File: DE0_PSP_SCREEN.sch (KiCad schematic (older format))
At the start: 11 parts, among them P1 PSP1000LCD, P2 DE0_GPIO_0, P3 DE0_GPIO_1, P4 PSP1000LED

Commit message: More sch
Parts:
- removed C? (x2): 4.7 uF, symbol CP1
- removed C? (x2): 100 n, symbol C
- removed C? (x2): 10 n, symbol C
- removed K?: CONN_3, symbol CONN_3
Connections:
- net labels added: Backlight_dimm, backlight_vcc
- wire segments 89 -> 88
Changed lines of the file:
@@
-EESchema Schematic File Version 2  date Wed 24 Oct 2012 22:22:57 CEST
+EESchema Schematic File Version 2  date Fri 26 Oct 2012 14:46:37 CEST
 LIBS:power
 LIBS:device
@@
 $Descr A4 11693 8268
 encoding utf-8
-Sheet 1 2
+Sheet 1 3
 Title ""
-Date "24 oct 2012"
+Date "26 oct 2012"
 Rev ""
 Comp ""
@@
 	9100 2950 9450 2950
 Wire Wire Line
-	9450 2950 9450 2050
+	9450 2950 9450 2500
+Wire Wire Line
+	9450 2500 9450 2050
 Wire Wire Line
 	9450 2050 9100 2050
@@
 Connection ~ 9450 2500
 Wire Wire Line
-	1700 1350 1700 1450
+	1700 1350 1700 1400
+Wire Wire Line
+	1700 1400 1700 1450
 Wire Wire Line
 	1700 1400 1200 1400
@@
 	2900 1350 3050 1350
 Wire Wire Line
-	3050 1350 3050 1450
+	3050 1350 3050 1400
+Wire Wire Line
+	3050 1400 3050 1450
 Wire Wire Line
 	3050 1400 3200 1400
@@
 	3200 1400 3200 1500
 Wire Wire Line
-	1700 1550 1700 1650
+	1700 1550 1700 1600
+Wire Wire Line
+	1700 1600 1700 1650
 Wire Wire Line
 	1700 1600 1550 1600
@@
 $EndComp
 Wire Wire Line
-	2900 1750 2900 1850
+	2900 1750 2900 1800
+Wire Wire Line
+	2900 1800 2900 1850
 Wire Wire Line
 	2900 1800 3300 1800
@@
 	1    0    0    -1
 $EndComp
-$Comp
-L CONN_3 K?
-U 1 1 5088053C
-P 6650 950
-F 0 "K?" V 6600 950 50  0000 C CNN
-F 1 "CONN_3" V 6700 950 40  0000 C CNN
-	1    6650 950
-	1    0    0    -1
-$EndComp
-Wire Wire Line
-	6300 850  6150 850
-Wire Wire Line
-	6100 950  6300 950
-$Comp
-L +5V #PWR?
-U 1 1 5088064A
-P 6150 850
-F 0 "#PWR?" H 6150 940 20  0001 C CNN
-F 1 "+5V" H 6150 940 30  0000 C CNN
-	1    6150 850
-	1    0    0    -1
-$EndComp
-$Comp
-L +5VA #PWR?
-U 1 1 50880716
-P 6100 950
-F 0 "#PWR?" H 6100 1080 20  0001 C CNN
-F 1 "+5VA" H 6100 1050 30  0000 C CNN
-	1    6100 950
-	1    0    0    -1
-$EndComp
-Wire Wire Line
-	6300 1050 6150 1050
-Wire Wire Line
-	6150 1050 6150 1100
-$Comp
-L GND #PWR?
-U 1 1 508807F0
-P 6150 1100
-F 0 "#PWR?" H 6150 1100 30  0001 C CNN
-F 1 "GND" H 6150 1030 30  0001 C CNN
-	1    6150 1100
-	1    0    0    -1
-$EndComp
-$Comp
-L CP1 C?
-U 1 1 508807FF
-P 2200 6750
-F 0 "C?" H 2250 6850 50  0000 L CNN
-F 1 "4.7 uF" H 2250 6650 50  0000 L CNN
-	1    2200 6750
-	1    0    0    -1
-$EndComp
-$Comp
-L C C?
-U 1 1 5088080E
-P 1900 6750
-F 0 "C?" H 1950 6850 50  0000 L CNN
-F 1 "100 n" H 1950 6650 50  0000 L CNN
-	1    1900 6750
-	1    0    0    -1
-$EndComp
-$Comp
-L C C?
-U 1 1 5088081D
-P 1600 6750
-F 0 "C?" H 1650 6850 50  0000 L CNN
-F 1 "10 n" H 1650 6650 50  0000 L CNN
-	1    1600 6750
-	1    0    0    -1
-$EndComp
-Wire Wire Line
-	1600 6550 2200 6550
-Connection ~ 1900 6550
-Wire Wire Line
-	1600 6950 2200 6950
-Connection ~ 1900 6950
-Wire Wire Line
-	1900 6950 1900 7150
-Wire Wire Line
-	1900 6550 1900 6350
-$Comp
-L +5VA #PWR?
-U 1 1 50880B57
-P 1900 6350
-F 0 "#PWR?" H 1900 6480 20  0001 C CNN
-F 1 "+5VA" H 1900 6450 30  0000 C CNN
-	1    1900 6350
-	1    0    0    -1
-$EndComp
-$Comp
-L GND #PWR?
-U 1 1 50880D2D
-P 1900 7150
-F 0 "#PWR?" H 1900 7150 30  0001 C CNN
-F 1 "GND" H 1900 7080 30  0001 C CNN
-	1    1900 7150
-	1    0    0    -1
-$EndComp
-$Comp
-L CP1 C?
-U 1 1 50880D3A
-P 3350 6750
-F 0 "C?" H 3400 6850 50  0000 L CNN
-F 1 "4.7 uF" H 3400 6650 50  0000 L CNN
-	1    3350 6750
-	1    0    0    -1
-$EndComp
-$Comp
-L C C?
-U 1 1 50880D40
-P 3050 6750
-F 0 "C?" H 3100 6850 50  0000 L CNN
-F 1 "100 n" H 3100 6650 50  0000 L CNN
-	1    3050 6750
-	1    0    0    -1
-$EndComp
-$Comp
-L C C?
-U 1 1 50880D46
-P 2750 6750
-F 0 "C?" H 2800 6850 50  0000 L CNN
-F 1 "10 n" H 2800 6650 50  0000 L CNN
-	1    2750 6750
-	1    0    0    -1
-$EndComp
-Wire Wire Line
-	2750 6550 3350 6550
-Connection ~ 3050 6550
-Wire Wire Line
-	2750 6950 3350 6950
-Connection ~ 3050 6950
-Wire Wire Line
-	3050 6950 3050 7150
-Wire Wire Line
-	3050 6550 3050 6350
-$Comp
-L GND #PWR?
-U 1 1 50880D58
-P 3050 7150
-F 0 "#PWR?" H 3050 7150 30  0001 C CNN
-F 1 "GND" H 3050 7080 30  0001 C CNN
-	1    3050 7150
-	1    0    0    -1
-$EndComp
-$Comp
-L 3V3 #PWR?
-U 1 1 50880D60
-P 3050 6350
-F 0 "#PWR?" H 3050 6450 40  0001 C CNN
-F 1 "3V3" H 3050 6475 40  0000 C CNN
-	1    3050 6350
-	1    0    0    -1
-$EndComp
 $Sheet
 S 5150 6000 1350 950
@@
 F0 "Sheet50883C15" 60
 F1 "file50883C15.sch" 60
+F2 "Vin" I L 5150 6150 60
+F3 "Vout_backlight" I R 6500 6150 60
+F4 "backlight_dimm" I L 5150 6300 60
+$EndSheet
+Wire Wire Line
+	1750 4000 1500 4000
+Wire Wire Line
+	1500 4000 1500 4050
+$Comp
+L GND #PWR?
+U 1 1 508A54D8
+P 1500 4050
+F 0 "#PWR?" H 1500 4050 30  0001 C CNN
+F 1 "GND" H 1500 3980 30  0001 C CNN
+	1    1500 4050
+	1    0    0    -1
+$EndComp
+Wire Wire Line
+	1750 4300 1600 4300
+Text Label 6500 6150 0    60   ~ 0
+backlight_vcc
+Text Label 1600 4300 2    60   ~ 0
+backlight_vcc
+Text Label 5150 6300 2    60   ~ 0
+Backlight_dimm
+Text Label 9250 4250 0    60   ~ 0
+Backlight_dimm
+Wire Wire Line
+	9100 4250 9250 4250
+Wire Wire Line
+	5150 6150 4950 6150
+Wire Wire Line
+	4950 6150 4950 6100
+$Comp
+L +5VA #PWR?
+U 1 1 508A5F9C
+P 4950 6100
+F 0 "#PWR?" H 4950 6230 20  0001 C CNN
+F 1 "+5VA" H 4950 6200 30  0000 C CNN
+	1    4950 6100
+	1    0    0    -1
+$EndComp
+$Sheet
+S 5250 3550 1300 1100
+U 508A654A
+F0 "Sheet508A6549" 60
+F1 "file508A6549.sch" 60
 $EndSheet
 $EndSCHEMATC

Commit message: Added power supply
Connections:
- net labels added: 3v3ENA, 3v3Vreg, 5Vreg, 5vENA, DE0_3v3, DE0_5v
- net labels removed: +5V, +5VA, 3V3
- wire segments 88 -> 90
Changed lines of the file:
@@
-EESchema Schematic File Version 2  date Fri 26 Oct 2012 14:46:37 CEST
+EESchema Schematic File Version 2  date Sun 28 Oct 2012 15:35:36 CET
 LIBS:power
 LIBS:device
@@
 Sheet 1 3
 Title ""
-Date "26 oct 2012"
+Date "28 oct 2012"
 Rev ""
 Comp ""
@@
 Comment4 ""
 $EndDescr
-$Comp
-L PSP1000LCD P1
-U 1 1 5086F785
-P 2300 2300
-F 0 "P1" H 2300 3400 70  0000 C CNN
-F 1 "PSP1000LCD" H 2300 1200 70  0000 C CNN
-	1    2300 2300
-	1    0    0    -1
-$EndComp
 Text Label 1550 1750 0    60   ~ 0
 R0
@@
 Text Label 3050 2050 2    60   ~ 0
 Vsync
-Text Label 9250 4050 2    60   ~ 0
+Text Label 9250 4050 0    60   ~ 0
 CK
-Text Label 8150 4150 0    60   ~ 0
+Text Label 8150 4150 2    60   ~ 0
 DISP
-Text Label 9250 4150 2    60   ~ 0
+Text Label 9250 4150 0    60   ~ 0
 Hsync
-Text Label 8150 4250 0    60   ~ 0
+Text Label 8150 4250 2    60   ~ 0
 Vsync
 $Comp
@@
 	1    0    0    -1
 $EndComp
-$Comp
-L 3V3 #PWR05
-U 1 1 5087FF71
-P 1550 1600
-F 0 "#PWR05" H 1550 1700 40  0001 C CNN
-F 1 "3V3" H 1550 1725 40  0000 C CNN
-	1    1550 1600
-	1    0    0    -1
-$EndComp
 Wire Wire Line
 	1700 1750 1550 1750
@@
 	9100 2850 9250 2850
 Wire Wire Line
-	9100 2950 9450 2950
-Wire Wire Line
-	9450 2950 9450 2500
-Wire Wire Line
-	9450 2500 9450 2050
+	9450 2950 9100 2950
+Wire Wire Line
+	9450 2050 9450 2950
 Wire Wire Line
 	9450 2050 9100 2050
@@
 Connection ~ 9450 2500
 Wire Wire Line
-	1700 1350 1700 1400
-Wire Wire Line
-	1700 1400 1700 1450
+	1700 1350 1700 1450
 Wire Wire Line
 	1700 1400 1200 1400
@@
 	8300 4250 8150 4250
 Wire Wire Line
-	2900 1450 3050 1450
+	3050 1450 2900 1450
 Wire Wire Line
 	2900 1350 3050 1350
 Wire Wire Line
-	3050 1350 3050 1400
-Wire Wire Line
-	3050 1400 3050 1450
+	3050 1350 3050 1450
 Wire Wire Line
 	3050 1400 3200 1400
@@
 	3200 1400 3200 1500
 Wire Wire Line
-	1700 1550 1700 1600
-Wire Wire Line
-	1700 1600 1700 1650
+	1700 1550 1700 1650
 Wire Wire Line
 	1700 1600 1550 1600
@@
 Wire Wire Line
 	8300 2950 8000 2950
-$Comp
-L 3V3 #PWR06
-U 1 1 5088002D
-P 8000 2950
-F 0 "#PWR06" H 8000 3050 40  0001 C CNN
-F 1 "3V3" H 8000 3075 40  0000 C CNN
-	1    8000 2950
-	1    0    0    -1
-$EndComp
 $Comp
 L PSP1000LED P4
@@
 $EndComp
 Wire Wire Line
-	2900 1750 2900 1800
-Wire Wire Line
-	2900 1800 2900 1850
+	2900 1750 2900 1850
 Wire Wire Line
 	2900 1800 3300 1800
 Connection ~ 2900 1800
-$Comp
-L +5VA #PWR?
-U 1 1 508804CB
-P 3300 1800
-F 0 "#PWR?" H 3300 1930 20  0001 C CNN
-F 1 "+5VA" H 3300 1900 30  0000 C CNN
-	1    3300 1800
-	1    0    0    -1
-$EndComp
 Wire Wire Line
 	8300 2050 8000 2050
-$Comp
-L +5V #PWR?
-U 1 1 5088052D
-P 8000 2050
-F 0 "#PWR?" H 8000 2140 20  0001 C CNN
-F 1 "+5V" H 8000 2140 30  0000 C CNN
-	1    8000 2050
-	1    0    0    -1
-$EndComp
 $Sheet
 S 5150 6000 1350 950
@@
 	1500 4000 1500 4050
 $Comp
-L GND #PWR?
+L GND #PWR05
 U 1 1 508A54D8
 P 1500 4050
-F 0 "#PWR?" H 1500 4050 30  0001 C CNN
+F 0 "#PWR05" H 1500 4050 30  0001 C CNN
 F 1 "GND" H 1500 3980 30  0001 C CNN
 	1    1500 4050
@@
 Wire Wire Line
 	4950 6150 4950 6100
-$Comp
-L +5VA #PWR?
-U 1 1 508A5F9C
-P 4950 6100
-F 0 "#PWR?" H 4950 6230 20  0001 C CNN
-F 1 "+5VA" H 4950 6200 30  0000 C CNN
-	1    4950 6100
-	1    0    0    -1
-$EndComp
 $Sheet
 S 5250 3550 1300 1100
@@
 F0 "Sheet508A6549" 60
 F1 "file508A6549.sch" 60
+F2 "V6-24" I L 5250 3700 60
+F3 "DE0_5v" I L 5250 3850 60
+F4 "DE0_3v3" I L 5250 4000 60
+F5 "5Vreg" I R 6550 3700 60
+F6 "3v3Vreg" I R 6550 3850 60
+F7 "5vENA" I L 5250 4250 60
+F8 "3v3ENA" I L 5250 4400 60
 $EndSheet
+Text Label 6550 3700 0    60   ~ 0
+5Vreg
+Text Label 3300 1800 0    60   ~ 0
+5Vreg
+Text Label 6550 3850 0    60   ~ 0
+3v3Vreg
+$Comp
+L PSP1000LCD P1
+U 1 1 5086F785
+P 2300 2300
+F 0 "P1" H 2300 3400 70  0000 C CNN
+F 1 "PSP1000LCD" H 2300 1200 70  0000 C CNN
+	1    2300 2300
+	1    0    0    -1
+$EndComp
+Text Label 1550 1600 2    60   ~ 0
+3v3Vreg
+Text Label 4950 6100 2    60   ~ 0
+5Vreg
+Text Label 8000 2950 2    60   ~ 0
+DE0_3v3
+Text Label 5250 4000 2    60   ~ 0
+DE0_3v3
+Text Label 8000 2050 2    60   ~ 0
+DE0_5v
+Text Label 5250 3850 2    60   ~ 0
+DE0_5v
+Text Label 5250 4250 2    60   ~ 0
+5vENA
+Text Label 5250 4400 2    60   ~ 0
+3v3ENA
+Wire Wire Line
+	8300 4350 8150 4350
+Wire Wire Line
+	9100 4350 9250 4350
+Text Label 9250 4350 0    60   ~ 0
+5vENA
+Text Label 8150 4350 2    60   ~ 0
+3v3ENA
+Wire Wire Line
+	9100 4550 9550 4550
+Wire Wire Line
+	9550 4550 9550 5450
+Wire Wire Line
+	9550 5450 9100 5450
+Wire Wire Line
+	9550 5000 9900 5000
+Wire Wire Line
+	9900 5000 9900 5250
+Connection ~ 9550 5000
+$Comp
+L GND #PWR06
+U 1 1 508D5FD4
+P 9900 5250
+F 0 "#PWR06" H 9900 5250 30  0001 C CNN
+F 1 "GND" H 9900 5180 30  0001 C CNN
+	1    9900 5250
+	1    0    0    -1
+$EndComp
 $EndSCHEMATC

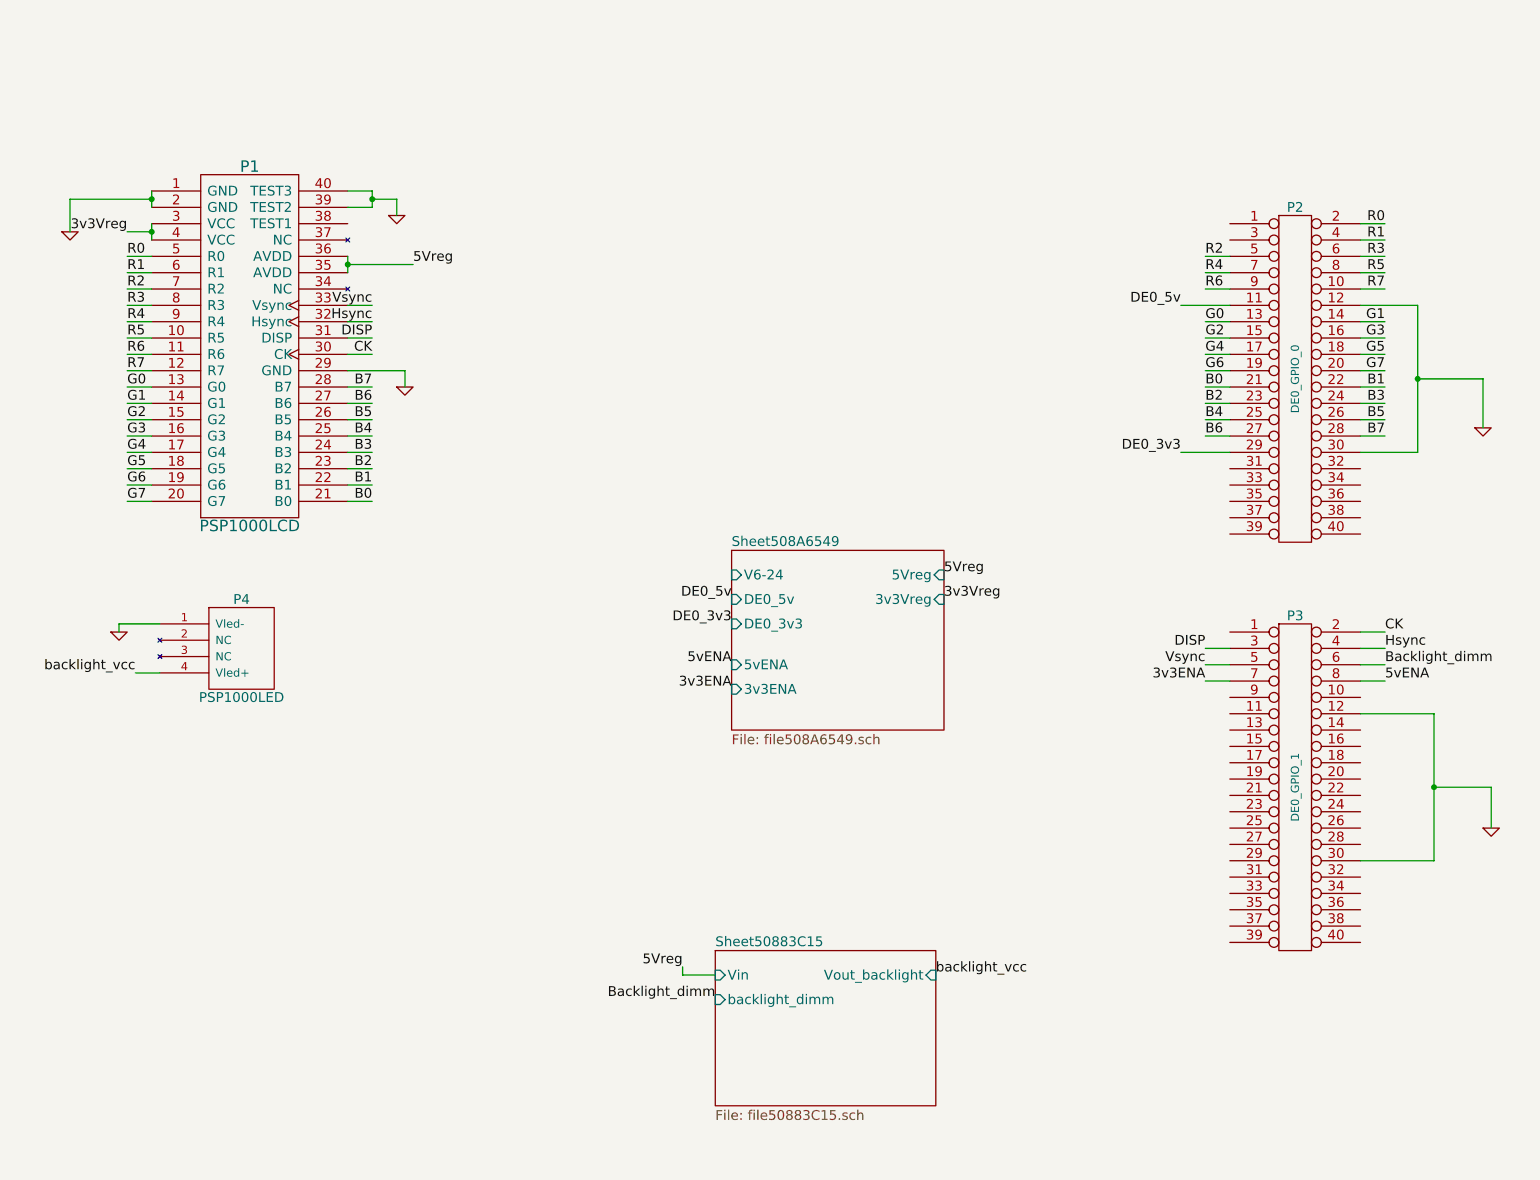
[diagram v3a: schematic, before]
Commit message: Added micro sd to main sch and more routing
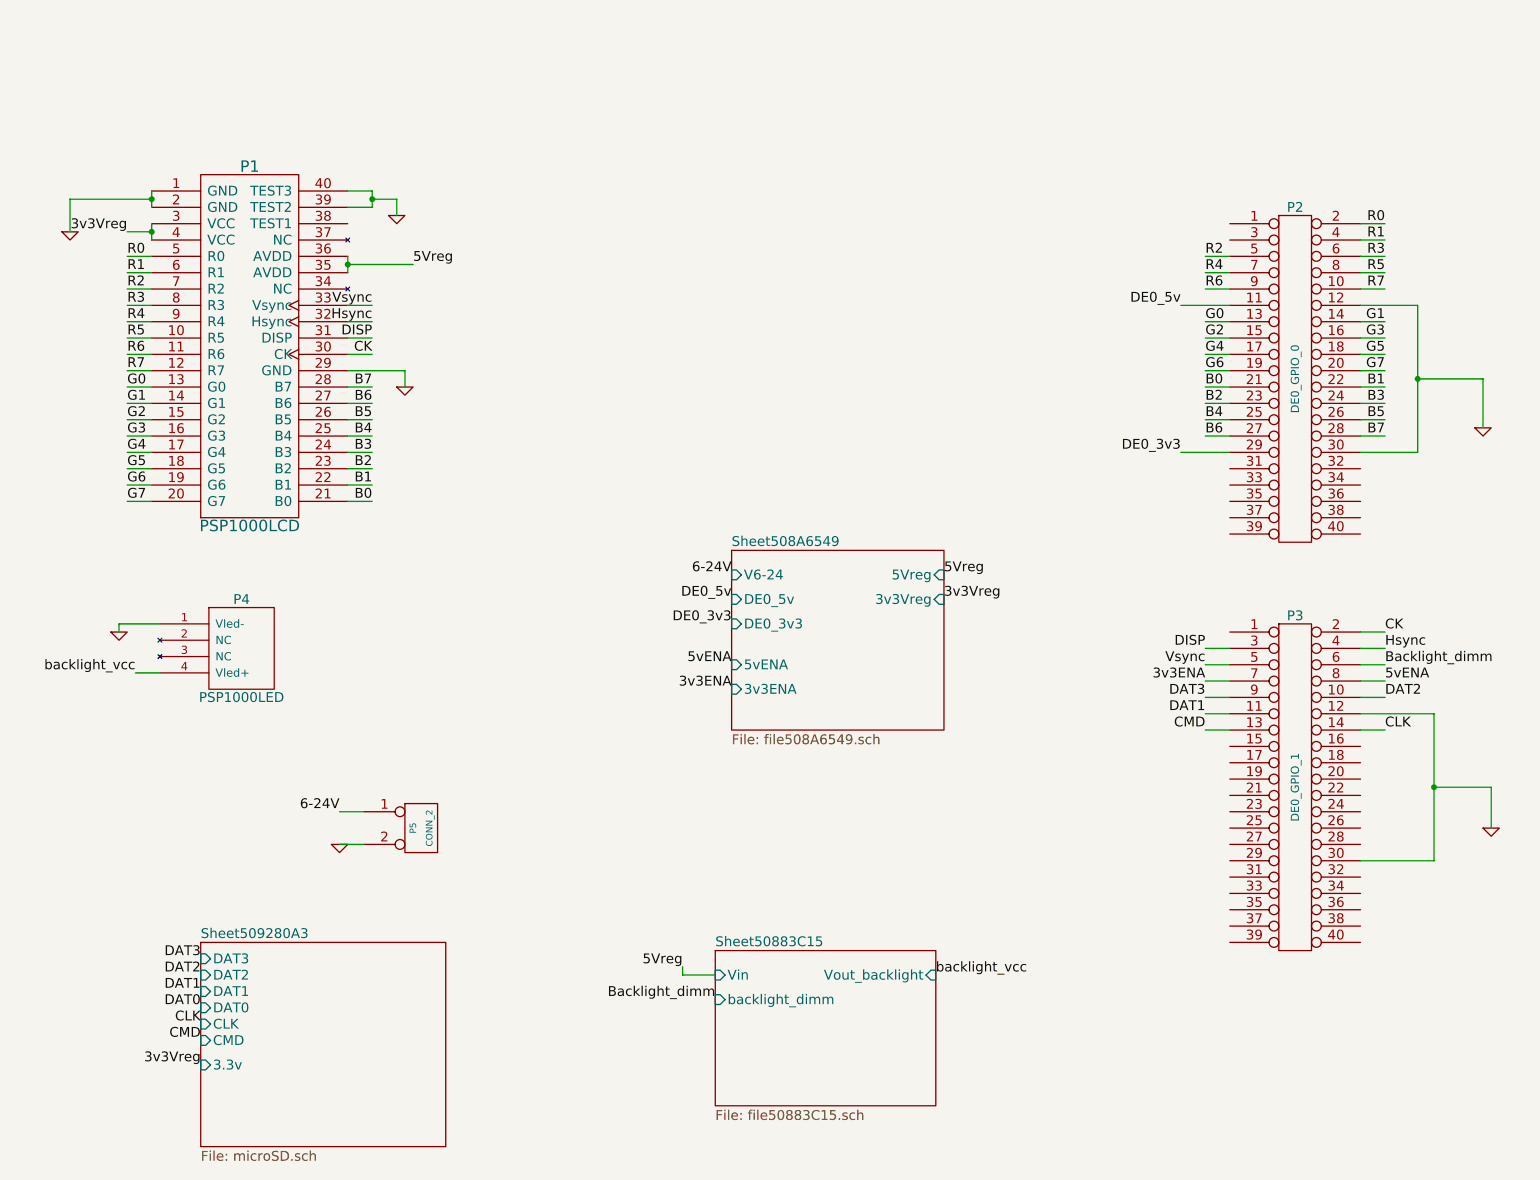
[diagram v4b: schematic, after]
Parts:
- added P5: CONN_2, symbol CONN_2
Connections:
- net GND: now also P5.2 (PM)
- net DAT2: now reaches P3.10 (P10)
- net DAT1: now reaches P3.11 (P11)
- net CMD: now reaches P3.13 (P13)
- net CLK: now reaches P3.14 (P14)
- net DAT3: now reaches P3.9 (P9)
- new net 6-24V: P5.1 (P1)
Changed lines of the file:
@@
-EESchema Schematic File Version 2  date Mon 29 Oct 2012 16:35:26 CET
+EESchema Schematic File Version 2  date Thu 01 Nov 2012 14:43:35 CET
 LIBS:power
 LIBS:device
@@
 LIBS:valves
 LIBS:own
+LIBS:opendous
 LIBS:DE0_PSP_SCREEN-cache
 EELAYER 27 0
@@
 $Descr A4 11693 8268
 encoding utf-8
-Sheet 1 3
+Sheet 1 4
 Title ""
-Date "29 oct 2012"
+Date "1 nov 2012"
 Rev ""
 Comp ""
@@
 	1    0    0    -1
 $EndComp
+$Comp
+L CONN_2 P5
+U 1 1 50927695
+P 3350 5250
+F 0 "P5" V 3300 5250 40  0000 C CNN
+F 1 "CONN_2" V 3400 5250 40  0000 C CNN
+	1    3350 5250
+	1    0    0    -1
+$EndComp
+Wire Wire Line
+	3000 5150 2850 5150
+Wire Wire Line
+	3000 5350 2850 5350
+Text Label 2850 5150 2    60   ~ 0
+6-24V
+$Comp
+L GND #PWR07
+U 1 1 50927877
+P 2850 5350
+F 0 "#PWR07" H 2850 5350 30  0001 C CNN
+F 1 "GND" H 2850 5280 30  0001 C CNN
+	1    2850 5350
+	1    0    0    -1
+$EndComp
+Text Label 5250 3700 2    60   ~ 0
+6-24V
+$Sheet
+S 2000 5950 1500 1250
+U 509280A4
+F0 "Sheet509280A3" 60
+F1 "microSD.sch" 60
+F2 "DAT3" I L 2000 6050 60
+F3 "DAT2" I L 2000 6150 60
+F4 "DAT1" I L 2000 6250 60
+F5 "DAT0" I L 2000 6350 60
+F6 "CLK" I L 2000 6450 60
+F7 "CMD" I L 2000 6550 60
+F8 "3.3v" I L 2000 6700 60
+$EndSheet
+Text Label 2000 6700 2    60   ~ 0
+3v3Vreg
+Text Label 2000 6050 2    60   ~ 0
+DAT3
+Text Label 2000 6150 2    60   ~ 0
+DAT2
+Text Label 2000 6250 2    60   ~ 0
+DAT1
+Text Label 2000 6350 2    60   ~ 0
+DAT0
+Text Label 2000 6450 2    60   ~ 0
+CLK
+Text Label 2000 6550 2    60   ~ 0
+CMD
+Text Label 8150 4450 2    60   ~ 0
+DAT3
+Text Label 9250 4450 0    60   ~ 0
+DAT2
+Text Label 8150 4550 2    60   ~ 0
+DAT1
+Text Label 9250 4650 0    60   ~ 0
+CLK
+Text Label 8150 4650 2    60   ~ 0
+CMD
+Wire Wire Line
+	8300 4450 8150 4450
+Wire Wire Line
+	9100 4450 9250 4450
+Wire Wire Line
+	8300 4550 8150 4550
+Wire Wire Line
+	9100 4650 9250 4650
+Wire Wire Line
+	8300 4650 8150 4650
 $EndSCHEMATC

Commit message: lots of changes
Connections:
- net GND: no longer P4.1 (Vled-)
- net Backlight_dimm renamed dimm
- net backlight_vcc renamed Sheet50883C15/Vout
- new net Vout-: P4.1 (Vled-)
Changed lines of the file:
@@
-EESchema Schematic File Version 2  date Thu 01 Nov 2012 14:43:35 CET
+EESchema Schematic File Version 2  date Thu 08 Nov 2012 00:17:25 CET
 LIBS:power
 LIBS:device
@@
 Sheet 1 4
 Title ""
-Date "1 nov 2012"
+Date "7 nov 2012"
 Rev ""
 Comp ""
@@
 F1 "file50883C15.sch" 60
 F2 "Vin" I L 5150 6150 60
-F3 "Vout_backlight" I R 6500 6150 60
-F4 "backlight_dimm" I L 5150 6300 60
+F3 "Vout" I L 5150 6600 60
+F4 "dimm" I L 5150 6400 60
+F5 "Vout-" I L 5150 6750 60
 $EndSheet
 Wire Wire Line
 	1750 4000 1500 4000
-Wire Wire Line
-	1500 4000 1500 4050
-$Comp
-L GND #PWR05
-U 1 1 508A54D8
-P 1500 4050
-F 0 "#PWR05" H 1500 4050 30  0001 C CNN
-F 1 "GND" H 1500 3980 30  0001 C CNN
-	1    1500 4050
-	1    0    0    -1
-$EndComp
-Wire Wire Line
-	1750 4300 1600 4300
-Text Label 6500 6150 0    60   ~ 0
-backlight_vcc
-Text Label 1600 4300 2    60   ~ 0
-backlight_vcc
-Text Label 5150 6300 2    60   ~ 0
-Backlight_dimm
 Text Label 9250 4250 0    60   ~ 0
-Backlight_dimm
+dimm
 Wire Wire Line
 	9100 4250 9250 4250
@@
 Wire Wire Line
 	8300 4650 8150 4650
+Wire Wire Line
+	1750 4300 1500 4300
+Wire Wire Line
+	1500 4300 1500 5450
+Wire Wire Line
+	1500 5450 3650 5450
+Wire Wire Line
+	3650 5450 3650 6600
+Wire Wire Line
+	3650 6600 5150 6600
+Text Label 5150 6400 2    60   ~ 0
+dimm
+Text Label 5150 6750 2    60   ~ 0
+Vout-
+Text Label 1500 4000 2    60   ~ 0
+Vout-
 $EndSCHEMATC
